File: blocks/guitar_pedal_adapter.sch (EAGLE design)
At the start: 33 parts, among them IC1 TL072P, IC2 LM7809

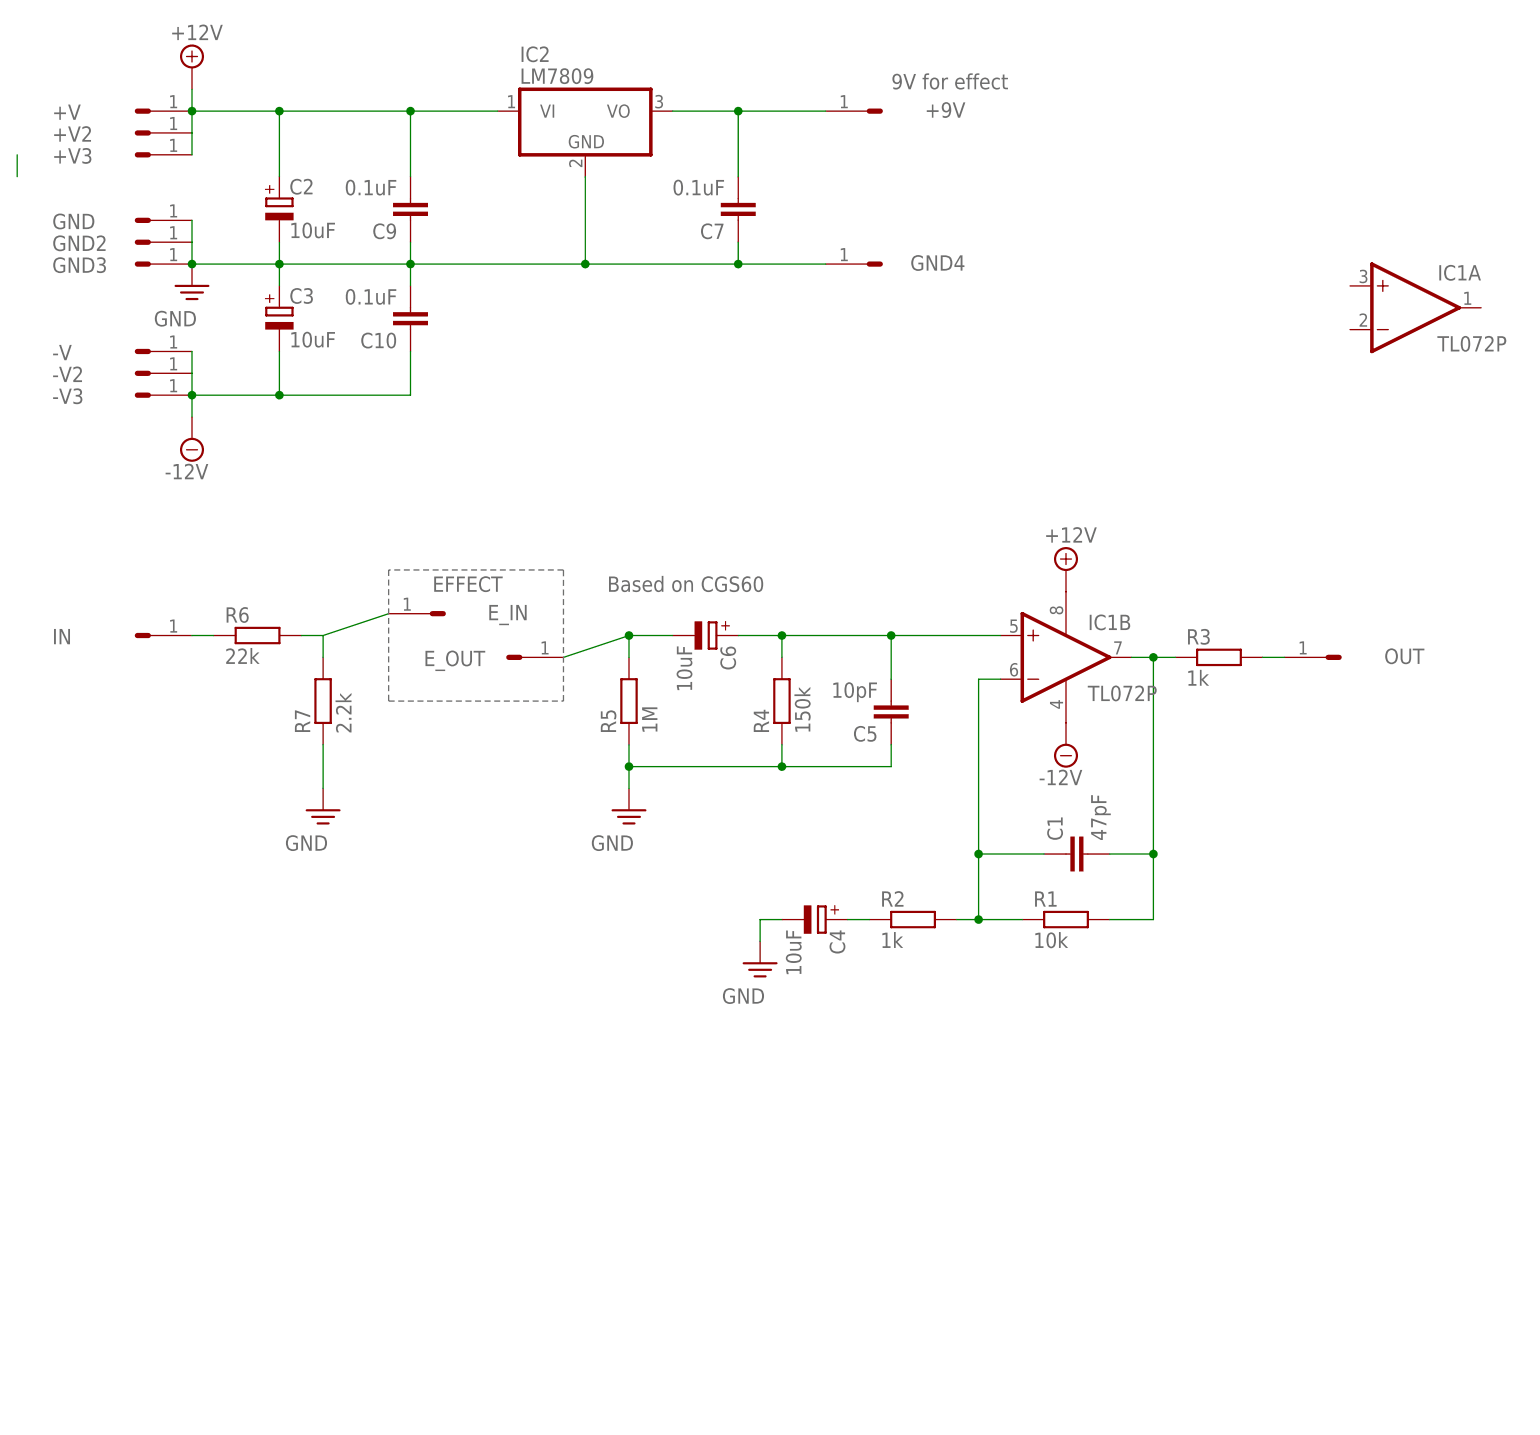
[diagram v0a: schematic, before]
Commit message: Added low pass/band pass filter block
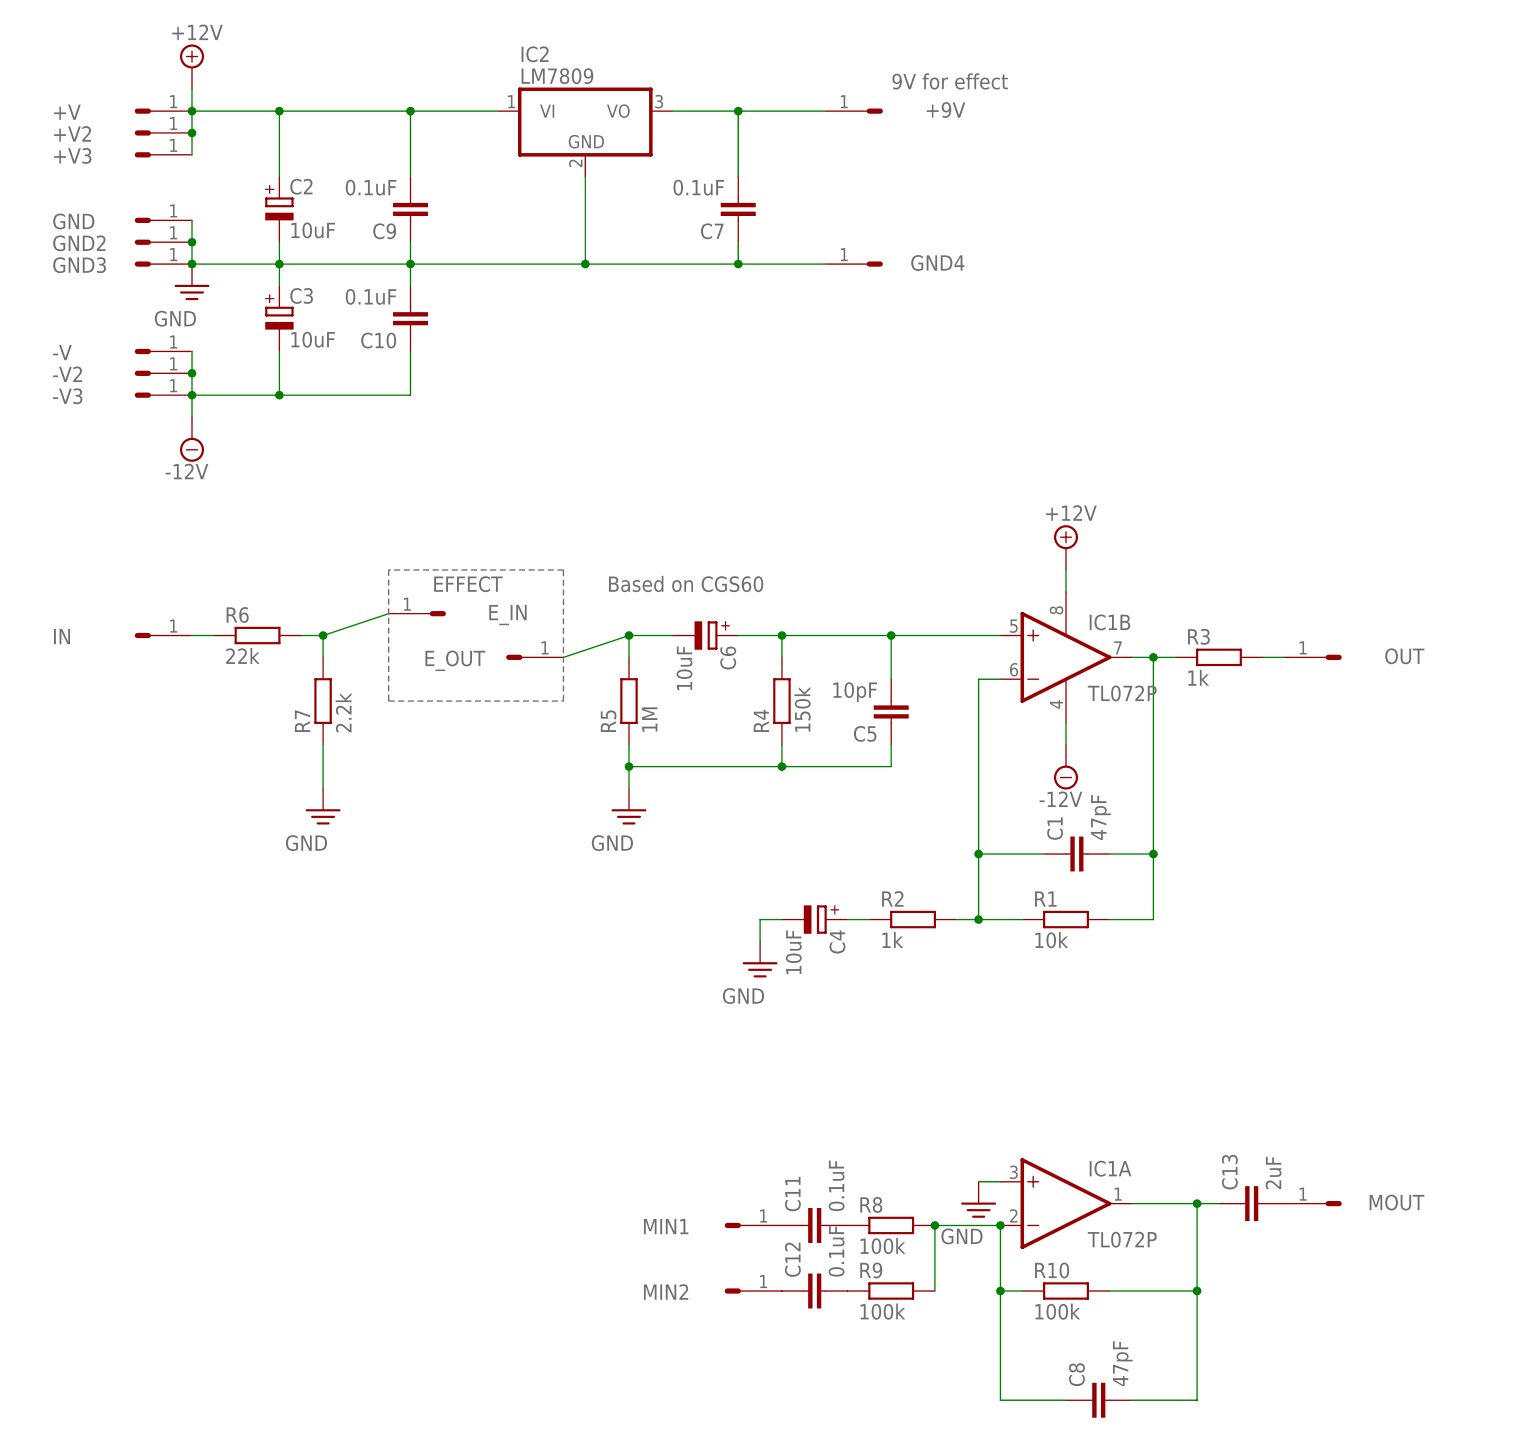
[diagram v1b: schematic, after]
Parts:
- added C11, C12: 0.1uF, capacitors:CAPACITORCERAMICDISC/5
- added C13: 2uF, capacitors:CAPACITORCERAMICDISC/5
- added C8: 47pF, capacitors:CAPACITORCERAMICDISC/5
- added MIN1, MIN2, MOUT: HEADER/MALE/01, connectors:HEADER/MALE/01
- added R10, R8, R9: 100k, resistors:RESISTORRESISTOR/UPRIGHT/7.5
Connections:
- new net N$10: C8.1, IC1A.-IN, R10.1, R8.2, R9.2
- new net N$11: C13.1, C8.2, IC1A.OUT, R10.2
- new net N$12: C13.2, MOUT.3
- new net N$13: C11.2, R8.1
- new net N$14: C12.2, R9.1
- new net N$15: C11.1, MIN1.3
- new net N$16: C12.1, MIN2.3
- net GND: now also IC1A.+IN
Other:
- moved on the sheet: IC1A
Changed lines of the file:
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@@
+<attribute name="SPICEPREFIX" value="X"/>
+</part>
+<part name="R8" library="resistors" deviceset="RESISTOR" device="RESISTOR/UPRIGHT/7.5" value="100k"/>
+<part name="R9" library="resistors" deviceset="RESISTOR" device="RESISTOR/UPRIGHT/7.5" value="100k"/>
+<part name="R10" library="resistors" deviceset="RESISTOR" device="RESISTOR/UPRIGHT/7.5" value="100k"/>
+<part name="C8" library="capacitors" deviceset="CAPACITOR" device="CERAMICDISC/5" value="47pF"/>
+<part name="SUPPLY9" library="supply" deviceset="GND" device="">
+<attribute name="SPICEPREFIX" value="G"/>
+</part>
+<part name="C11" library="capacitors" deviceset="CAPACITOR" device="CERAMICDISC/5" value="0.1uF"/>
+<part name="C12" library="capacitors" deviceset="CAPACITOR" device="CERAMICDISC/5" value="0.1uF"/>
+<part name="MIN1" library="connectors" deviceset="HEADER/MALE/01" device="">
+<attribute name="SPICEPREFIX" value="X"/>
+</part>
+<part name="MIN2" library="connectors" deviceset="HEADER/MALE/01" device="">
+<attribute name="SPICEPREFIX" value="X"/>
+</part>
+<part name="C13" library="capacitors" deviceset="CAPACITOR" device="CERAMICDISC/5" value="2uF"/>
+<part name="MOUT" library="connectors" deviceset="HEADER/MALE/01" device="">
 <attribute name="SPICEPREFIX" value="X"/>
 </part>
@@
 </plain>
 <instances>
-<instance part="IC1" gate="A" x="139.7" y="-20.32"/>
+<instance part="IC1" gate="A" x="99.06" y="-124.46"/>
 <instance part="IC1" gate="P" x="99.06" y="-60.96"/>
 <instance part="IC1" gate="B" x="99.06" y="-60.96"/>
@@
 <instance part="SUPPLY4" gate="GND" x="63.5" y="-96.52"/>
 <instance part="R3" gate="G$1" x="116.84" y="-60.96"/>
-<instance part="SUPPLY5" gate="+12V" x="99.06" y="-50.8"/>
-<instance part="SUPPLY6" gate="G$1" x="99.06" y="-71.12"/>
+<instance part="SUPPLY5" gate="+12V" x="99.06" y="-48.26"/>
+<instance part="SUPPLY6" gate="G$1" x="99.06" y="-73.66"/>
 <instance part="C5" gate="G$1" x="78.74" y="-68.58" rot="R180"/>
 <instance part="R4" gate="G$1" x="66.04" y="-66.04" rot="R90"/>
@@
 <instance part="+9V" gate="HEADER" x="73.66" y="2.54" rot="R180"/>
 <instance part="GND4" gate="HEADER" x="73.66" y="-15.24" rot="R180"/>
+<instance part="R8" gate="G$1" x="78.74" y="-127"/>
+<instance part="R9" gate="G$1" x="78.74" y="-134.62"/>
+<instance part="R10" gate="G$1" x="99.06" y="-134.62"/>
+<instance part="C8" gate="G$1" x="101.6" y="-147.32" rot="R90"/>
+<instance part="SUPPLY9" gate="GND" x="88.9" y="-124.46"/>
+<instance part="C11" gate="G$1" x="68.58" y="-127" rot="R90"/>
+<instance part="C12" gate="G$1" x="68.58" y="-134.62" rot="R90"/>
+<instance part="MIN1" gate="HEADER" x="63.5" y="-127"/>
+<instance part="MIN2" gate="HEADER" x="63.5" y="-134.62"/>
+<instance part="C13" gate="G$1" x="119.38" y="-124.46" rot="R90"/>
+<instance part="MOUT" gate="HEADER" x="127" y="-124.46" rot="R180"/>
 </instances>
 <busses>
@@
 <wire x1="60.96" y1="-15.24" x2="71.12" y2="-15.24" width="0.1524" layer="91"/>
 <junction x="60.96" y="-15.24"/>
-</segment>
-<segment>
-<wire x1="-22.86" y1="-5.08" x2="-22.86" y2="-2.54" width="0.1524" layer="91"/>
+<junction x="-2.54" y="-12.7"/>
 </segment>
 <segment>
@@
 <wire x1="48.26" y1="-76.2" x2="48.26" y2="-73.66" width="0.1524" layer="91"/>
 <junction x="48.26" y="-73.66"/>
+</segment>
+<segment>
+<pinref part="IC1" gate="A" pin="+IN"/>
+<pinref part="SUPPLY9" gate="GND" pin="PE"/>
+<wire x1="88.9" y1="-121.92" x2="91.44" y2="-121.92" width="0.1524" layer="91"/>
 </segment>
 </net>
@@
 <wire x1="22.86" y1="2.54" x2="33.02" y2="2.54" width="0.1524" layer="91"/>
 <junction x="22.86" y="2.54"/>
+<junction x="-2.54" y="0"/>
 </segment>
 <segment>
 <pinref part="IC1" gate="P" pin="V+"/>
 <pinref part="SUPPLY5" gate="+12V" pin="+12V"/>
+<wire x1="99.06" y1="-50.8" x2="99.06" y2="-53.34" width="0.1524" layer="91"/>
 </segment>
 </net>
@@
 <wire x1="22.86" y1="-30.48" x2="22.86" y2="-25.4" width="0.1524" layer="91"/>
 <junction x="7.62" y="-30.48"/>
+<junction x="-2.54" y="-27.94"/>
 </segment>
 <segment>
 <pinref part="IC1" gate="P" pin="V-"/>
 <pinref part="SUPPLY6" gate="G$1" pin="-12V"/>
+<wire x1="99.06" y1="-71.12" x2="99.06" y2="-68.58" width="0.1524" layer="91"/>
 </segment>
 </net>
@@
 <wire x1="12.7" y1="-58.42" x2="20.32" y2="-55.88" width="0.1524" layer="91"/>
 <pinref part="E_IN" gate="HEADER" pin="3"/>
+<junction x="12.7" y="-58.42"/>
 </segment>
 </net>
@@
 </segment>
 </net>
+<net name="N$10" class="0">
+<segment>
+<pinref part="R9" gate="G$1" pin="2"/>
+<pinref part="R8" gate="G$1" pin="2"/>
+<wire x1="83.82" y1="-134.62" x2="83.82" y2="-127" width="0.1524" layer="91"/>
+<pinref part="IC1" gate="A" pin="-IN"/>
+<wire x1="83.82" y1="-127" x2="91.44" y2="-127" width="0.1524" layer="91"/>
+<pinref part="R10" gate="G$1" pin="1"/>
+<wire x1="93.98" y1="-134.62" x2="91.44" y2="-134.62" width="0.1524" layer="91"/>
+<wire x1="91.44" y1="-134.62" x2="91.44" y2="-127" width="0.1524" layer="91"/>
+<pinref part="C8" gate="G$1" pin="1"/>
+<wire x1="99.06" y1="-147.32" x2="91.44" y2="-147.32" width="0.1524" layer="91"/>
+<wire x1="91.44" y1="-147.32" x2="91.44" y2="-134.62" width="0.1524" layer="91"/>
+<junction x="91.44" y="-134.62"/>
+<junction x="91.44" y="-127"/>
+<junction x="83.82" y="-127"/>
+</segment>
+</net>
+<net name="N$11" class="0">
+<segment>
+<pinref part="R10" gate="G$1" pin="2"/>
+<wire x1="104.14" y1="-134.62" x2="114.3" y2="-134.62" width="0.1524" layer="91"/>
+<pinref part="IC1" gate="A" pin="OUT"/>
+<wire x1="114.3" y1="-134.62" x2="114.3" y2="-124.46" width="0.1524" layer="91"/>
+<wire x1="114.3" y1="-124.46" x2="106.68" y2="-124.46" width="0.1524" layer="91"/>
+<pinref part="C8" gate="G$1" pin="2"/>
+<wire x1="106.68" y1="-147.32" x2="114.3" y2="-147.32" width="0.1524" layer="91"/>
+<wire x1="114.3" y1="-147.32" x2="114.3" y2="-134.62" width="0.1524" layer="91"/>
+<pinref part="C13" gate="G$1" pin="1"/>
+<wire x1="116.84" y1="-124.46" x2="114.3" y2="-124.46" width="0.1524" layer="91"/>
+<junction x="114.3" y="-134.62"/>
+<junction x="114.3" y="-124.46"/>
+</segment>
+</net>
+<net name="N$13" class="0">
+<segment>
+<pinref part="R8" gate="G$1" pin="1"/>
+<pinref part="C11" gate="G$1" pin="2"/>
+</segment>
+</net>
+<net name="N$14" class="0">
+<segment>
+<pinref part="R9" gate="G$1" pin="1"/>
+<pinref part="C12" gate="G$1" pin="2"/>
+</segment>
+</net>
+<net name="N$15" class="0">
+<segment>
+<pinref part="C11" gate="G$1" pin="1"/>
+<pinref part="MIN1" gate="HEADER" pin="3"/>
+</segment>
+</net>
+<net name="N$16" class="0">
+<segment>
+<pinref part="C12" gate="G$1" pin="1"/>
+<pinref part="MIN2" gate="HEADER" pin="3"/>
+</segment>
+</net>
+<net name="N$12" class="0">
+<segment>
+<pinref part="C13" gate="G$1" pin="2"/>
+<pinref part="MOUT" gate="HEADER" pin="3"/>
+</segment>
+</net>
